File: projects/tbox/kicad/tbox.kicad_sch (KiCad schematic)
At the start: 0 parts

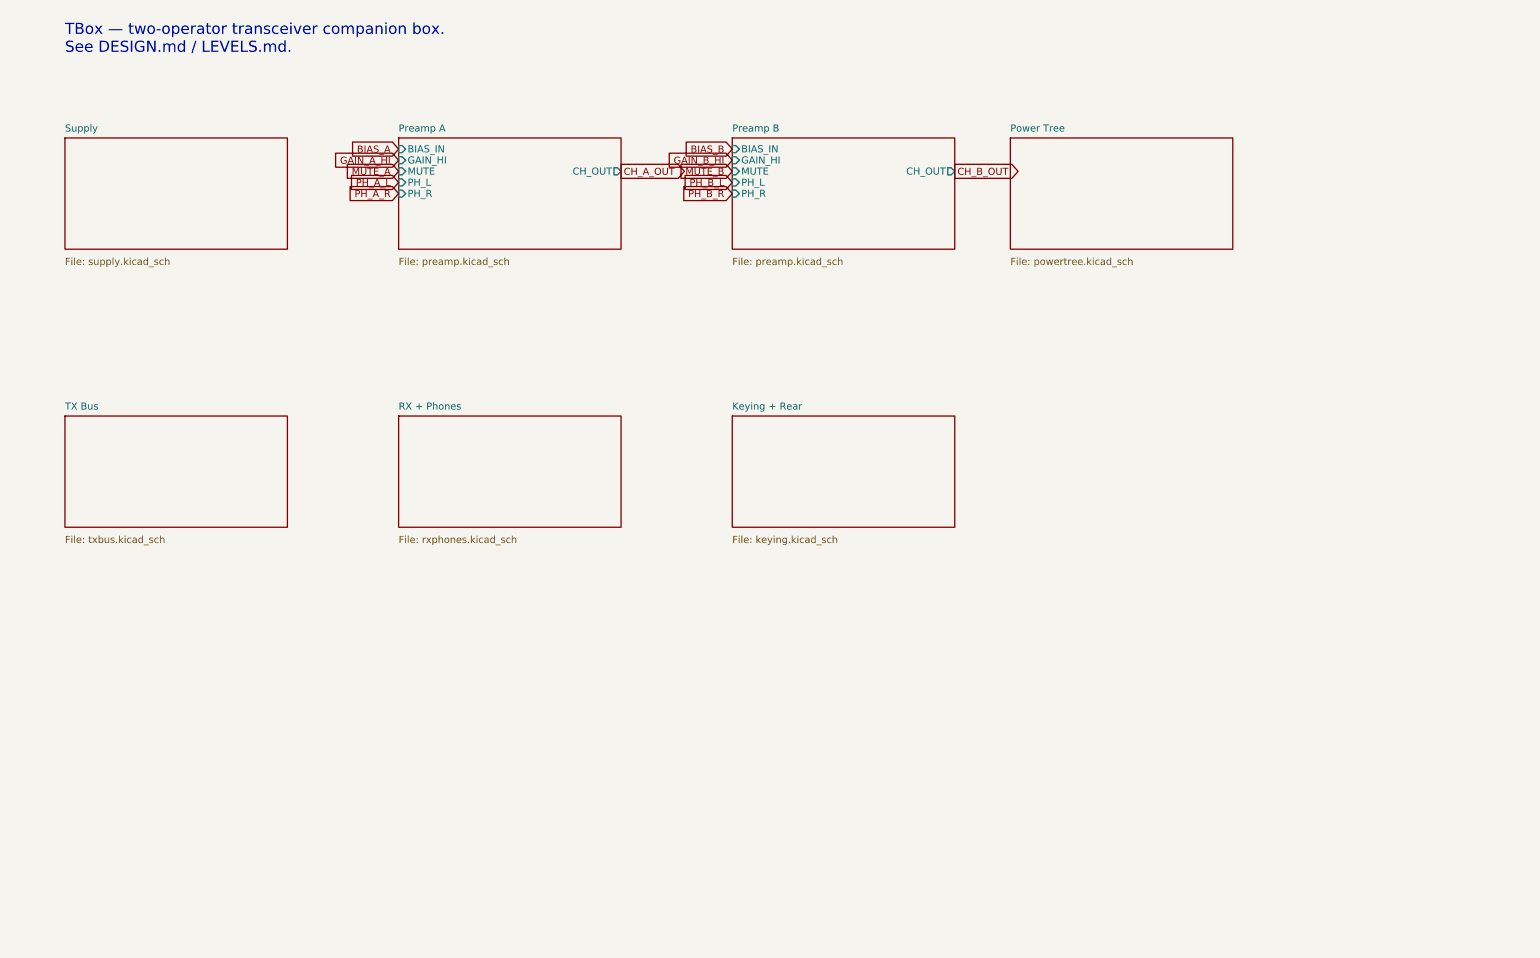
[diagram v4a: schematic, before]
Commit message: Re-cut the hierarchy by board: front / control / rear sheets, ribbons on the root
The functional sheets no longer map to the physical boards, so the root
now holds one sheet per PCB and the wires on it are the two ribbon
cables.  The control board is parallel to the 13-degree top slope, so
the front jacks need their own vertical board; the preamps go with them
so mic level never crosses a connector.

- keying -> Keying Logic (control) + Rear I/O (rear)
  txbus  -> TX Sum / Intercom (control) + Rig Out (rear)
  rxphones -> Monitor / Phones (control) + RX In (rear); phones jacks
  redrawn on the Front board.  Preamp loses its level pot (redrawn on
  TX Sum) and is instanced under the Front board; Supply under Rear.
- Cross-board nets are hierarchical labels threaded through sheet pins
  and the ribbon connectors J901/J902 (front-control) and J903/J904
  (control-rear), 2x13 IDC, straight-through, GND on every third pin;
  GAIN/BIAS pass through the control board.  Rails ride the ribbons as
  power symbols with local decoupling at each connector.
- Two deliberate net changes: the front PTT buttons now sit after the
  jack beads (PTT_x_IN), and phones jack sleeves plus the TRRS common
  return to board GND instead of CHASSIS -- a chassis return would put
  headphone current through the single tie and the rear ribbon ground,
  in series with the mic reference.  Every other net is unchanged
  (netlist partition verified: 209 nets, only those two differ).
- tools/check_boards.py: every net spanning two boards must pass
  through a ribbon connector on each; both ends of each ribbon must
  carry the same net pin for pin.  It caught the pass-through nets being
  control-local labels on the first cut.
- Panel-mount Powerpole to J1; side view gains the front board; DESIGN
  mechanical section rewritten; CLAUDE.md hierarchy rule; TODO layout
  items (snap-apart panel, ribbon DRC exclusions).
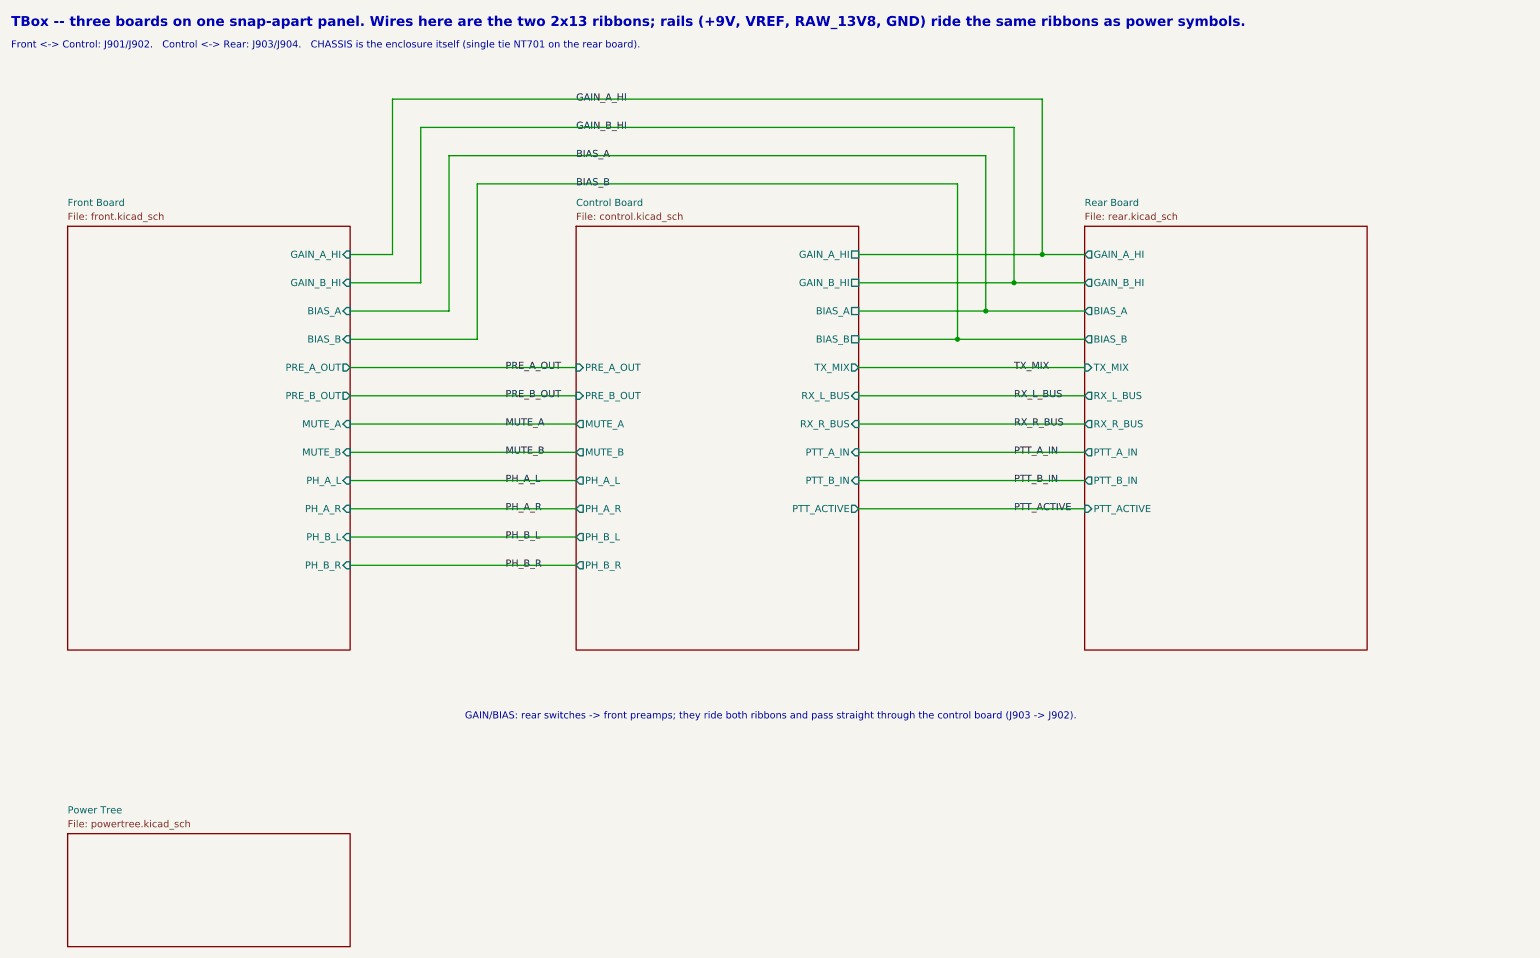
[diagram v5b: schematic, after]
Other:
- removed sheet Keying + Rear
- removed sheet Preamp A
- removed sheet Preamp B
- removed sheet RX + Phones
- removed sheet Supply
- removed sheet TX Bus
- added sheet Control Board (control.kicad_sch)
- added sheet Front Board (front.kicad_sch)
- added sheet Rear Board (rear.kicad_sch)
- note added: "Front <-> Control: J901/J902. Control <-> Rear: J903/J904. CHASSIS is the enclosure itself (single tie NT701 on the rear board)."
- note added: "GAIN/BIAS: rear switches -> front preamps; they ride both ribbons and pass straight through the control board (J903 -> J902)."
- note added: "TBox -- three boards on one snap-apart panel. Wires here are the two 2x13 ribbons; rails (+9V, VREF, RAW_13V8, GND) ride the same ribbons as power symbols."
- note removed: "TBox — two-operator transceiver companion box. See DESIGN.md / LEVELS.md."

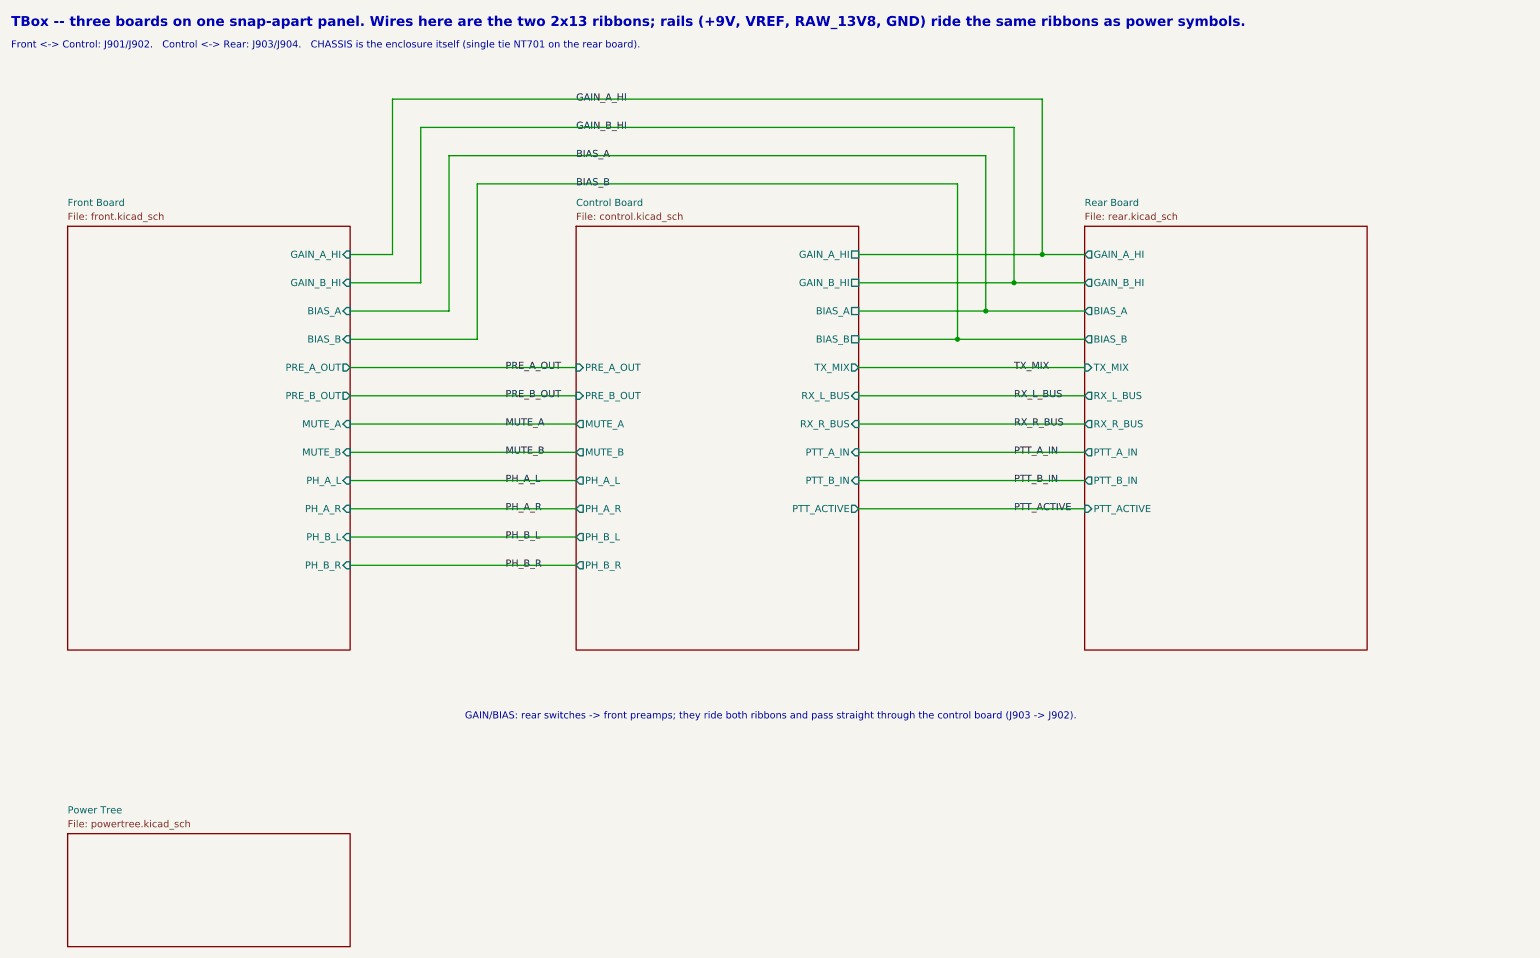
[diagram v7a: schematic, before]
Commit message: Rename refdes mentions in notes and docs to the board-coded numbering
Table-driven: the old->new map was derived from symbol UUIDs across the
annotation commit (619 instances, checked one-to-one and per board), and
only exact whole tokens from that table were replaced, in sheet notes,
connector Values, DESIGN.md, TODO.md and power_tree.json.  The one range
("J901-J904") and the one instance-specific ref in the shared Mute sheet
were rewritten by hand.  Power tree regenerated (loads now grouped by
board).  Netlist identical to the annotated baseline.
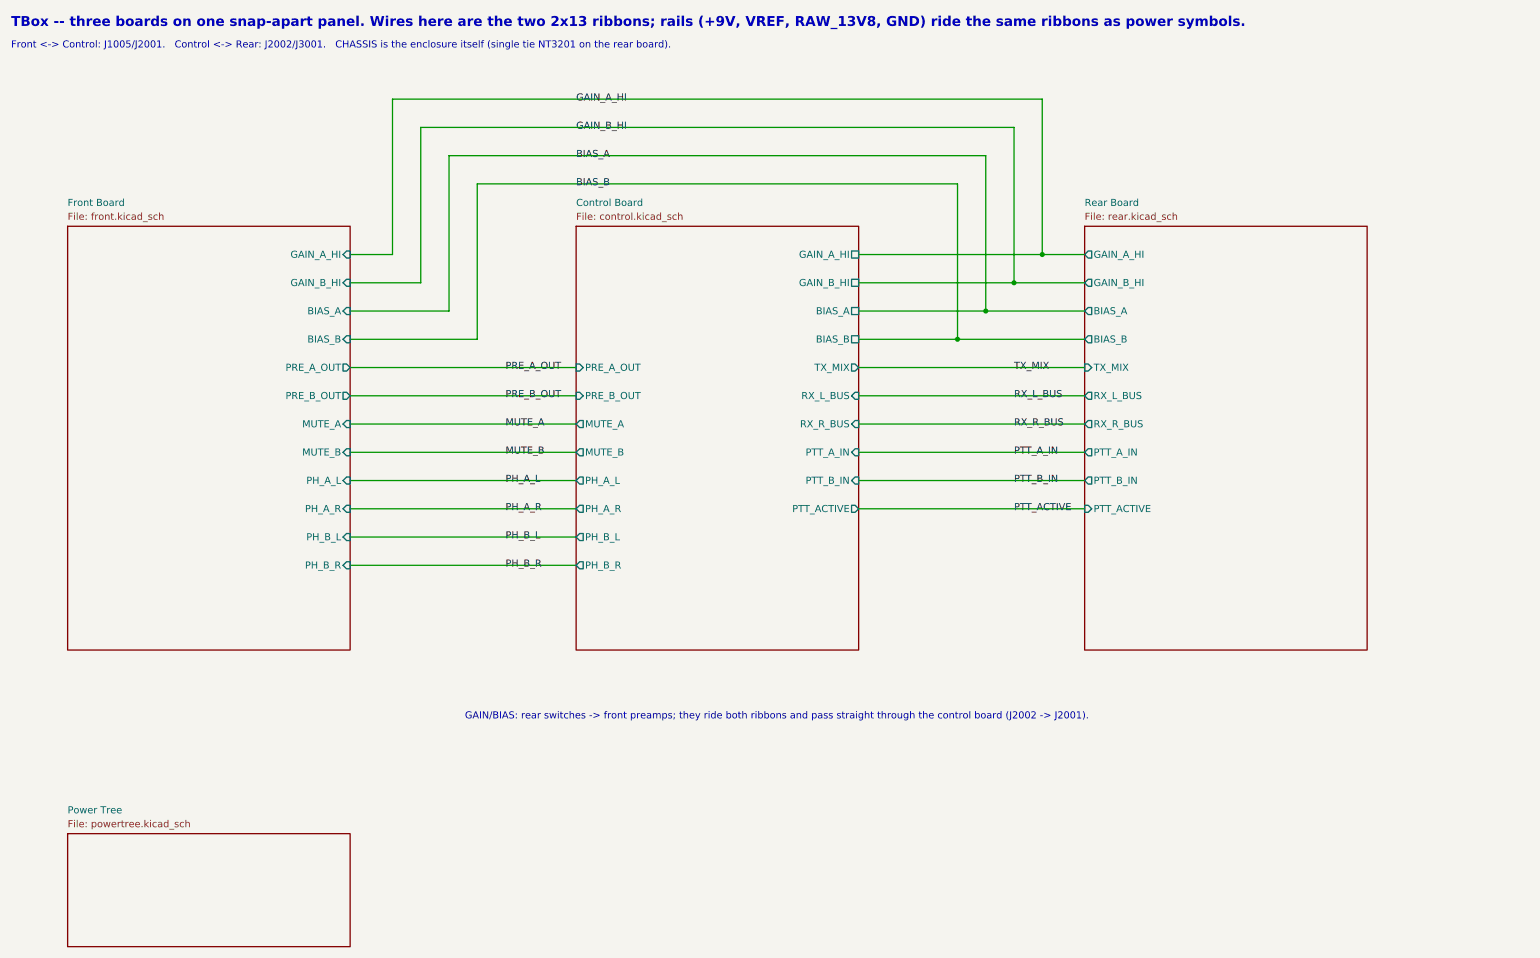
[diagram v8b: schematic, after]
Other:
- note added: "Front <-> Control: J1005/J2001. Control <-> Rear: J2002/J3001. CHASSIS is the enclosure itself (single tie NT3201 on the rear board)."
- note added: "GAIN/BIAS: rear switches -> front preamps; they ride both ribbons and pass straight through the control board (J2002 -> J2001)."
- note removed: "Front <-> Control: J901/J902. Control <-> Rear: J903/J904. CHASSIS is the enclosure itself (single tie NT701 on the rear board)."
- note removed: "GAIN/BIAS: rear switches -> front preamps; they ride both ribbons and pass straight through the control board (J903 -> J902)."
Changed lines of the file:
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@@
 		(company "TBox")
 	)
-	(text "Front <-> Control: J901/J902.   Control <-> Rear: J903/J904.   CHASSIS is the enclosure itself (single tie NT701 on the rear board)."
+	(text "Front <-> Control: J1005/J2001.   Control <-> Rear: J2002/J3001.   CHASSIS is the enclosure itself (single tie NT3201 on the rear board)."
 		(exclude_from_sim no)
 		(at 20.32 24.13 0)
@@
 		)
 	)
-	(text "GAIN/BIAS: rear switches -> front preamps; they ride both ribbons and pass straight through the control board (J903 -> J902)."
+	(text "GAIN/BIAS: rear switches -> front preamps; they ride both ribbons and pass straight through the control board (J2002 -> J2001)."
 		(exclude_from_sim no)
 		(at 101.92 144.78 0)
